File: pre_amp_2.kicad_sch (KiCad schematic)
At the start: 57 parts, among them J1 IN, J11 SW2_3, J12 SW2_1, J13 SW2_4, J14 SW5_3, J15 VR5_1, J16 OUT, J2 Vin, J3 GND, J4 VR1_1, J5 VR2_1, J6 VR1_3, J7 VR1_2, J8 SW1, J9 SW2, SW1 bright, SW2 SW_SP3T, U1 TL072, U2 ICL7660

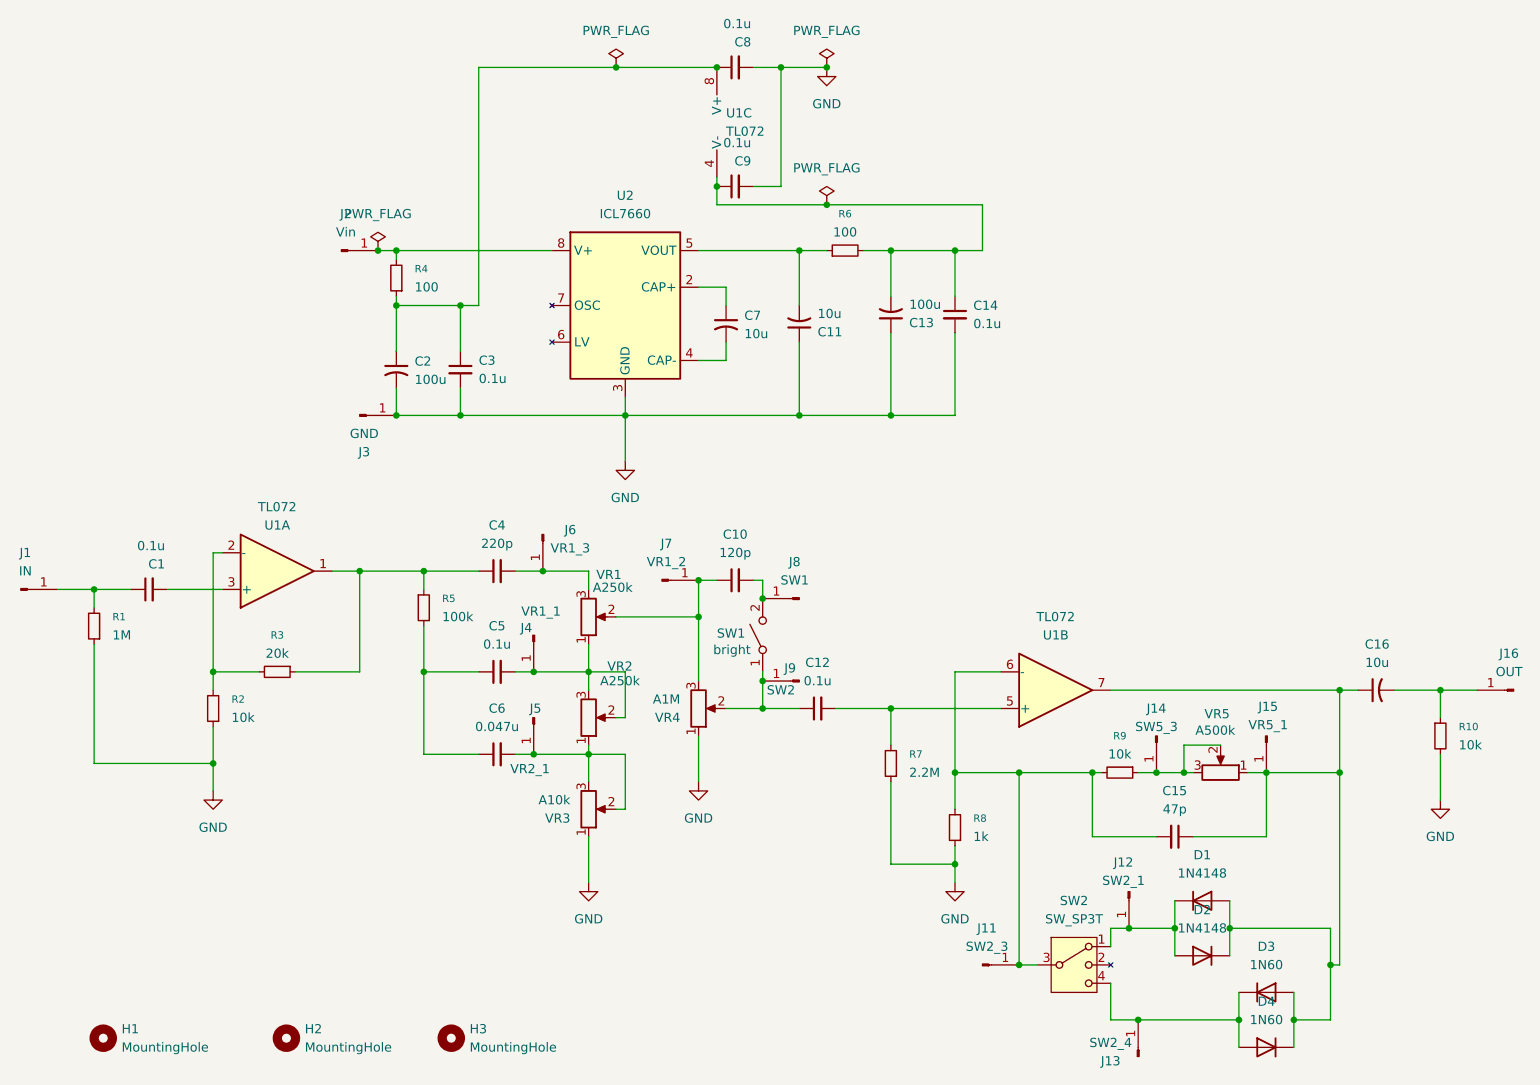
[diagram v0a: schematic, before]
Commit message: LED用の抵抗を追加
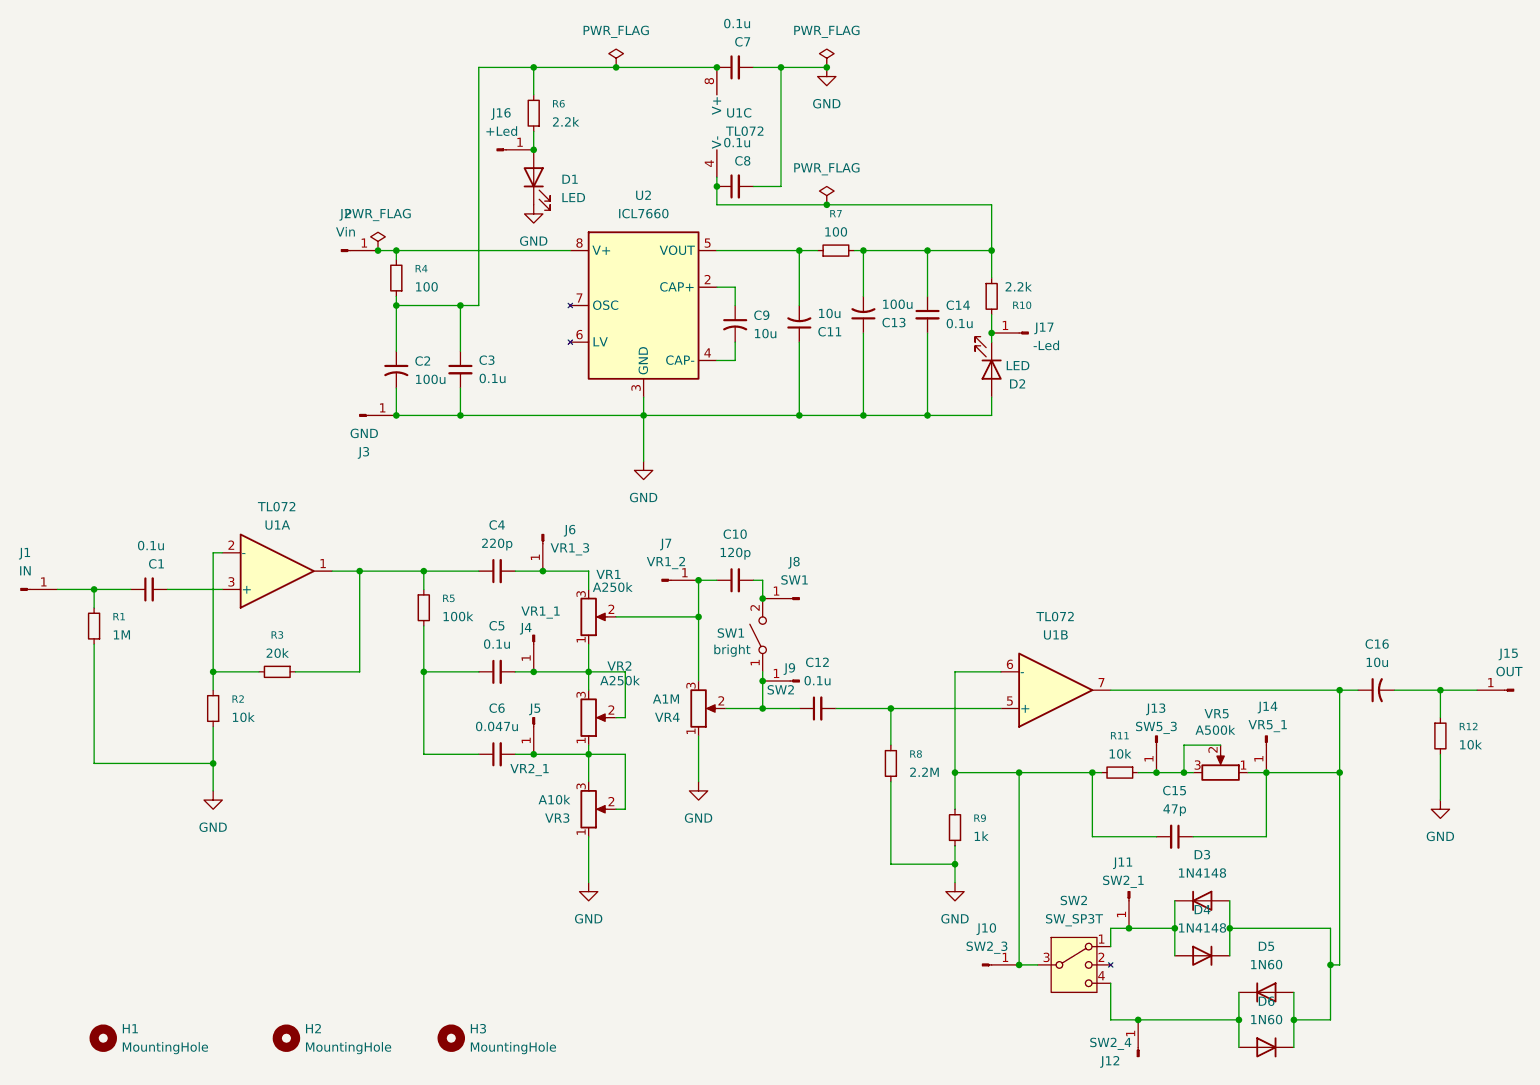
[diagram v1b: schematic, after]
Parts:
- added D1, D2: LED, symbol Device:LED
- added J16: +Led, Connector_PinHeader_2.54mm:PinHeader_1x01_P2.54mm_Vertical, symbol Connector:Conn_01x01_Pin
- added J17: -Led, Connector_PinHeader_2.54mm:PinHeader_1x01_P2.54mm_Vertical, symbol Connector:Conn_01x01_Pin
- added R10, R6: 2.2k, Resistor_THT:R_Axial_DIN0204_L3.6mm_D1.6mm_P7.62mm_Horizontal, symbol Device:R_Small
- renumbered C8 to C7, C9 to C8, C7 to C9, D1 to D3, D2 to D4, D3 to D5, D4 to D6, J11 to J10, J12 to J11, J13 to J12, J14 to J13, J15 to J14, J16 to J15, R9 to R11, R10 to R12, R6 to R7, R7 to R8, R8 to R9
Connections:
- net GND: now also D1.1 (K), D2.2 (A)
- net at C2.1, C3.1, C7.1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: now also R6.2
- net at C13.2, C14.1, C8.1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: now also R10.1
- new net: D2.1 (K), J17.1 (Pin_1), R10.2
- new net: D1.2 (A), J16.1 (Pin_1), R6.1
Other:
- moved on the sheet: C13, C14, C9, R7, U2

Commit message: 配置をやり直す
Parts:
- removed D1, D2: LED, symbol Device:LED
- removed J16: +Led, Connector_PinHeader_2.54mm:PinHeader_1x01_P2.54mm_Vertical, symbol Connector:Conn_01x01_Pin
- removed J17: -Led, Connector_PinHeader_2.54mm:PinHeader_1x01_P2.54mm_Vertical, symbol Connector:Conn_01x01_Pin
- removed R10, R6: 2.2k, Resistor_THT:R_Axial_DIN0204_L3.6mm_D1.6mm_P7.62mm_Horizontal, symbol Device:R_Small
- removed R12: 10k, Resistor_THT:R_Axial_DIN0204_L3.6mm_D1.6mm_P7.62mm_Horizontal, symbol Device:R_Small
- added J2: GND2, Connector_PinHeader_2.54mm:PinHeader_1x01_P2.54mm_Vertical, symbol Connector:Conn_01x01_Pin
- J10: renamed from J9; value SW2 -> SW1_2
- J9: renamed from J8; value SW1 -> SW1_1
- R1, R2, R3, R4, R5: footprint Resistor_THT:R_Axial_DIN0204_L3.6mm_D1.6mm_P7.62mm_Horizontal -> Resistor_THT:R_Axial_DIN0204_L3.6mm_D1.6mm_P2.54mm_Vertical
- R6: renamed from R7; footprint Resistor_THT:R_Axial_DIN0204_L3.6mm_D1.6mm_P7.62mm_Horizontal -> Resistor_THT:R_Axial_DIN0204_L3.6mm_D1.6mm_P2.54mm_Vertical
- renumbered D3 to D1, D4 to D2, D5 to D3, D6 to D4, J10 to J11, J11 to J12, J12 to J13, J13 to J14, J14 to J15, J15 to J16, J2 to J3, J3 to J4, J4 to J5, J5 to J6, J6 to J7, J7 to J8, R8 to R7, R9 to R8, R11 to R9
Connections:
- net GND: no longer R1.1, R2.1, R7.1, R8.1, VR3.1, VR4.1
- new net GND2: J2.1 (Pin_1), R1.1, R2.1, R7.1, R8.1, VR3.1, VR4.1

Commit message: 電源と入力のGNDを分離して配置を修正
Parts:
- removed J8: VR1_2, Connector_PinHeader_2.54mm:PinHeader_1x01_P2.54mm_Vertical, symbol Connector:Conn_01x01_Pin
- C10: footprint Capacitor_THT:C_Disc_D3.8mm_W2.6mm_P2.50mm -> (none)
- J13: renamed from J14; value SW5_3 -> VR5_3
- J8: renamed from J9; footprint Connector_PinHeader_2.54mm:PinHeader_1x01_P2.54mm_Vertical -> (none)
- J9: renamed from J10; footprint Connector_PinHeader_2.54mm:PinHeader_1x01_P2.54mm_Vertical -> (none)
- R4, R6: footprint Resistor_THT:R_Axial_DIN0204_L3.6mm_D1.6mm_P2.54mm_Vertical -> Resistor_THT:R_Axial_DIN0204_L3.6mm_D1.6mm_P7.62mm_Horizontal
- renumbered J11 to J10, J12 to J11, J13 to J12, J15 to J14, J16 to J15
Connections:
- net at C10.1, VR1.2, VR4.3: now also J8.1 (Pin_1)
- net at C10.2, SW1.2 (B): no longer J8.1 (Pin_1)
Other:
- moved on the sheet: J8
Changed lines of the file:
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@@
 	)
 	(junction
-		(at 123.19 95.25)
-		(diameter 0)
-		(color 0 0 0 0)
-	)
-	(junction
 		(at 182.88 138.43)
 		(diameter 0)
@@
 	)
 	(junction
-		(at 132.08 92.71)
+		(at 123.19 90.17)
 		(diameter 0)
 		(color 0 0 0 0)
@@
 	)
 	(junction
-		(at 123.19 90.17)
-		(diameter 0)
-		(color 0 0 0 0)
-	)
-	(junction
 		(at 111.76 19.05)
 		(diameter 0)
@@
 	)
 	(junction
+		(at 123.19 95.25)
+		(diameter 0)
+		(color 0 0 0 0)
+	)
+	(junction
 		(at 134.62 19.05)
 		(diameter 0)
@@
 	(wire
 		(pts
+			(xy 123.19 90.17) (xy 123.19 95.25)
+		)
+		(stroke
+			(width 0)
+			(type default)
+		)
+	)
+	(wire
+		(pts
 			(xy 111.76 19.05) (xy 125.73 19.05)
 		)
@@
 	(wire
 		(pts
+			(xy 123.19 90.17) (xy 125.73 90.17)
+		)
+		(stroke
+			(width 0)
+			(type default)
+		)
+	)
+	(wire
+		(pts
+			(xy 132.08 90.17) (xy 132.08 92.71)
+		)
+		(stroke
+			(width 0)
+			(type default)
+		)
+	)
+	(wire
+		(pts
 			(xy 49.53 91.44) (xy 57.15 91.44)
 		)
@@
 	(wire
 		(pts
-			(xy 125.73 90.17) (xy 123.19 90.17)
-		)
-		(stroke
-			(width 0)
-			(type default)
-		)
-	)
-	(wire
-		(pts
 			(xy 125.73 44.45) (xy 137.16 44.45)
 		)
@@
 	(wire
 		(pts
-			(xy 123.19 90.17) (xy 123.19 95.25)
-		)
-		(stroke
-			(width 0)
-			(type default)
-		)
-	)
-	(wire
-		(pts
 			(xy 186.69 116.84) (xy 190.5 116.84)
 		)
@@
 	(wire
 		(pts
-			(xy 132.08 92.71) (xy 132.08 90.17)
-		)
-		(stroke
-			(width 0)
-			(type default)
-		)
-	)
-	(wire
-		(pts
 			(xy 123.19 95.25) (xy 123.19 104.14)
 		)
@@
 			)
 		)
-		(property "Footprint" "Capacitor_THT:C_Disc_D3.8mm_W2.6mm_P2.50mm"
+		(property "Footprint" ""
 			(at 128.27 90.17 0)
 			(effects
@@
 		(on_board yes)
 		(dnp no)
-		(property "Reference" "J13"
+		(property "Reference" "J12"
 			(at 180.34 156.845 90)
 			(effects
@@
 			(project "pre_amp_2"
 				(path "/a24a43ce-b78c-4b02-8ea5-638bfbce1c81"
-					(reference "J13")
+					(reference "J12")
 					(unit 1)
 				)
@@
 		(on_board yes)
 		(dnp no)
-		(property "Reference" "J11"
+		(property "Reference" "J10"
 			(at 163.195 138.43 0)
 			(effects
@@
 			(project "pre_amp_2"
 				(path "/a24a43ce-b78c-4b02-8ea5-638bfbce1c81"
-					(reference "J11")
+					(reference "J10")
 					(unit 1)
 				)
@@
 		(on_board yes)
 		(dnp no)
-		(property "Reference" "J12"
+		(property "Reference" "J11"
 			(at 182.118 129.286 90)
 			(effects
@@
 			(project "pre_amp_2"
 				(path "/a24a43ce-b78c-4b02-8ea5-638bfbce1c81"
-					(reference "J12")
+					(reference "J11")
 					(unit 1)
 				)
@@
 	(symbol
 		(lib_id "Connector:Conn_01x01_Pin")
-		(at 137.16 92.71 0)
-		(mirror y)
+		(at 118.11 90.17 0)
 		(unit 1)
 		(exclude_from_sim no)
@@
 		(on_board yes)
 		(dnp no)
-		(property "Reference" "J9"
-			(at 136.525 87.63 0)
+		(property "Reference" "J8"
+			(at 118.745 85.09 0)
 			(effects
 				(font
@@
 		)
 		(property "Value" "SW1_1"
-			(at 136.525 90.17 0)
+			(at 118.745 87.63 0)
 			(effects
 				(font
@@
 			)
 		)
-		(property "Footprint" "Connector_PinHeader_2.54mm:PinHeader_1x01_P2.54mm_Vertical"
-			(at 137.16 92.71 0)
+		(property "Footprint" ""
+			(at 118.11 90.17 0)
 			(effects
 				(font
@@
 		)
 		(property "Datasheet" "~"
-			(at 137.16 92.71 0)
+			(at 118.11 90.17 0)
 			(effects
 				(font
@@
 		)
 		(property "Description" "Generic connector, single row, 01x01, script generated"
-			(at 137.16 92.71 0)
+			(at 118.11 90.17 0)
 			(effects
 				(font
@@
 			(project "pre_amp_2"
 				(path "/a24a43ce-b78c-4b02-8ea5-638bfbce1c81"
-					(reference "J9")
+					(reference "J8")
 					(unit 1)
 				)
@@
 		(on_board yes)
 		(dnp no)
-		(property "Reference" "J15"
+		(property "Reference" "J14"
 			(at 202.184 107.696 90)
 			(effects
@@
 			(project "pre_amp_2"
 				(path "/a24a43ce-b78c-4b02-8ea5-638bfbce1c81"
-					(reference "J15")
-					(unit 1)
-				)
-			)
-		)
-	)
-	(symbol
-		(lib_id "Connector:Conn_01x01_Pin")
-		(at 118.11 90.17 0)
-		(unit 1)
-		(exclude_from_sim no)
-		(in_bom yes)
-		(on_board yes)
-		(dnp no)
-		(property "Reference" "J8"
-			(at 118.745 85.09 0)
-			(effects
-				(font
-					(size 1.27 1.27)
-				)
-			)
-		)
-		(property "Value" "VR1_2"
-			(at 118.745 87.63 0)
-			(effects
-				(font
-					(size 1.27 1.27)
-				)
-			)
-		)
-		(property "Footprint" "Connector_PinHeader_2.54mm:PinHeader_1x01_P2.54mm_Vertical"
-			(at 118.11 90.17 0)
-			(effects
-				(font
-					(size 1.27 1.27)
-				)
-				(hide yes)
-			)
-		)
-		(property "Datasheet" "~"
-			(at 118.11 90.17 0)
-			(effects
-				(font
-					(size 1.27 1.27)
-				)
-				(hide yes)
-			)
-		)
-		(property "Description" "Generic connector, single row, 01x01, script generated"
-			(at 118.11 90.17 0)
-			(effects
-				(font
-					(size 1.27 1.27)
-				)
-				(hide yes)
-			)
-		)
-		(pin "1"
-		)
-		(instances
-			(project "pre_amp_2"
-				(path "/a24a43ce-b78c-4b02-8ea5-638bfbce1c81"
-					(reference "J8")
+					(reference "J14")
 					(unit 1)
 				)
@@
 			)
 		)
-		(property "Footprint" "Resistor_THT:R_Axial_DIN0204_L3.6mm_D1.6mm_P2.54mm_Vertical"
+		(property "Footprint" "Resistor_THT:R_Axial_DIN0204_L3.6mm_D1.6mm_P7.62mm_Horizontal"
 			(at 81.28 48.26 0)
 			(effects
@@
 		(on_board yes)
 		(dnp no)
-		(property "Reference" "J10"
+		(property "Reference" "J9"
 			(at 135.89 102.362 0)
 			(effects
@@
 			)
 		)
-		(property "Footprint" "Connector_PinHeader_2.54mm:PinHeader_1x01_P2.54mm_Vertical"
+		(property "Footprint" ""
 			(at 137.16 104.14 0)
 			(effects
@@
 			(project "pre_amp_2"
 				(path "/a24a43ce-b78c-4b02-8ea5-638bfbce1c81"
-					(reference "J10")
+					(reference "J9")
 					(unit 1)
 				)
@@
 		(dnp no)
 		(fields_autoplaced yes)
-		(property "Reference" "J16"
+		(property "Reference" "J15"
 			(at 235.585 100.33 0)
 			(effects
@@
 			(project "pre_amp_2"
 				(path "/a24a43ce-b78c-4b02-8ea5-638bfbce1c81"
-					(reference "J16")
+					(reference "J15")
 					(unit 1)
 				)
@@
 			)
 		)
-		(property "Footprint" "Resistor_THT:R_Axial_DIN0204_L3.6mm_D1.6mm_P2.54mm_Vertical"
+		(property "Footprint" "Resistor_THT:R_Axial_DIN0204_L3.6mm_D1.6mm_P7.62mm_Horizontal"
 			(at 142.24 44.45 0)
 			(effects
@@
 		(on_board yes)
 		(dnp no)
-		(property "Reference" "J14"
+		(property "Reference" "J13"
 			(at 186.69 107.95 90)
 			(effects
@@
 			)
 		)
-		(property "Value" "SW5_3"
+		(property "Value" "VR5_3"
 			(at 186.69 110.49 90)
 			(effects
@@
 			(project "pre_amp_2"
 				(path "/a24a43ce-b78c-4b02-8ea5-638bfbce1c81"
-					(reference "J14")
+					(reference "J13")
 					(unit 1)
 				)

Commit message: 配線の接続先を修正
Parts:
- removed J8: SW1_1, symbol Connector:Conn_01x01_Pin
- J6: value VR2_1 -> VR3_3
- J9: value SW1_2 -> VR4_2
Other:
- moved on the sheet: J9
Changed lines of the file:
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@@
 	)
 	(junction
-		(at 132.08 107.95)
-		(diameter 0)
-		(color 0 0 0 0)
-	)
-	(junction
 		(at 154.94 44.45)
 		(diameter 0)
@@
 	)
 	(junction
+		(at 132.08 107.95)
+		(diameter 0)
+		(color 0 0 0 0)
+	)
+	(junction
 		(at 107.95 102.87)
 		(diameter 0)
@@
 	)
 	(junction
-		(at 149.86 107.95)
+		(at 135.89 107.95)
 		(diameter 0)
 		(color 0 0 0 0)
 	)
 	(junction
-		(at 76.2 88.9)
+		(at 149.86 107.95)
 		(diameter 0)
 		(color 0 0 0 0)
 	)
 	(junction
-		(at 55.88 102.87)
+		(at 76.2 88.9)
 		(diameter 0)
 		(color 0 0 0 0)
 	)
 	(junction
-		(at 137.16 44.45)
+		(at 55.88 102.87)
 		(diameter 0)
 		(color 0 0 0 0)
 	)
 	(junction
-		(at 123.19 90.17)
+		(at 137.16 44.45)
 		(diameter 0)
 		(color 0 0 0 0)
@@
 	)
 	(junction
-		(at 132.08 104.14)
-		(diameter 0)
-		(color 0 0 0 0)
-	)
-	(junction
 		(at 186.69 116.84)
 		(diameter 0)
@@
 	(wire
 		(pts
-			(xy 132.08 107.95) (xy 137.16 107.95)
+			(xy 127 107.95) (xy 132.08 107.95)
 		)
 		(stroke
@@
 	(wire
 		(pts
+			(xy 132.08 102.87) (xy 132.08 107.95)
+		)
+		(stroke
+			(width 0)
+			(type default)
+		)
+	)
+	(wire
+		(pts
 			(xy 92.71 19.05) (xy 111.76 19.05)
 		)
@@
 	(wire
 		(pts
-			(xy 127 107.95) (xy 132.08 107.95)
-		)
-		(stroke
-			(width 0)
-			(type default)
-		)
-	)
-	(wire
-		(pts
 			(xy 39.37 113.03) (xy 39.37 115.57)
 		)
@@
 	(wire
 		(pts
+			(xy 135.89 107.95) (xy 137.16 107.95)
+		)
+		(stroke
+			(width 0)
+			(type default)
+		)
+	)
+	(wire
+		(pts
 			(xy 107.95 113.03) (xy 107.95 114.3)
 		)
@@
 	(wire
 		(pts
-			(xy 132.08 107.95) (xy 132.08 104.14)
-		)
-		(stroke
-			(width 0)
-			(type default)
-		)
-	)
-	(wire
-		(pts
 			(xy 90.17 67.31) (xy 115.57 67.31)
 		)
@@
 	(wire
 		(pts
-			(xy 184.15 151.13) (xy 198.12 151.13)
+			(xy 132.08 107.95) (xy 135.89 107.95)
 		)
 		(stroke
@@
 	(wire
 		(pts
-			(xy 212.09 105.41) (xy 214.63 105.41)
+			(xy 184.15 151.13) (xy 198.12 151.13)
 		)
 		(stroke
@@
 	(wire
 		(pts
-			(xy 55.88 115.57) (xy 55.88 110.49)
+			(xy 212.09 105.41) (xy 214.63 105.41)
 		)
 		(stroke
@@
 	(wire
 		(pts
-			(xy 132.08 104.14) (xy 132.08 102.87)
+			(xy 55.88 115.57) (xy 55.88 110.49)
 		)
 		(stroke
@@
 			)
 		)
-		(property "Value" "VR2_1"
+		(property "Value" "VR3_3"
 			(at 99.822 116.332 90)
 			(effects
@@
 	)
 	(symbol
-		(lib_id "Connector:Conn_01x01_Pin")
-		(at 118.11 90.17 0)
-		(unit 1)
-		(exclude_from_sim no)
-		(in_bom yes)
-		(on_board yes)
-		(dnp no)
-		(property "Reference" "J8"
-			(at 118.745 85.09 0)
-			(effects
-				(font
-					(size 1.27 1.27)
-				)
-			)
-		)
-		(property "Value" "SW1_1"
-			(at 118.745 87.63 0)
-			(effects
-				(font
-					(size 1.27 1.27)
-				)
-			)
-		)
-		(property "Footprint" ""
-			(at 118.11 90.17 0)
-			(effects
-				(font
-					(size 1.27 1.27)
-				)
-				(hide yes)
-			)
-		)
-		(property "Datasheet" "~"
-			(at 118.11 90.17 0)
-			(effects
-				(font
-					(size 1.27 1.27)
-				)
-				(hide yes)
-			)
-		)
-		(property "Description" "Generic connector, single row, 01x01, script generated"
-			(at 118.11 90.17 0)
-			(effects
-				(font
-					(size 1.27 1.27)
-				)
-				(hide yes)
-			)
-		)
-		(pin "1"
-		)
-		(instances
-			(project "pre_amp_2"
-				(path "/a24a43ce-b78c-4b02-8ea5-638bfbce1c81"
-					(reference "J8")
-					(unit 1)
-				)
-			)
-		)
-	)
-	(symbol
 		(lib_id "Device:C_Small_US")
 		(at 146.05 53.34 0)
@@
 	(symbol
 		(lib_id "Connector:Conn_01x01_Pin")
-		(at 137.16 104.14 0)
-		(mirror y)
+		(at 135.89 113.03 270)
+		(mirror x)
 		(unit 1)
 		(exclude_from_sim no)
@@
 		(dnp no)
 		(property "Reference" "J9"
-			(at 135.89 102.362 0)
+			(at 134.366 114.046 90)
 			(effects
 				(font
@@
 			)
 		)
-		(property "Value" "SW1_2"
-			(at 134.62 105.41 0)
+		(property "Value" "VR4_2"
+			(at 135.636 116.332 90)
 			(effects
 				(font
@@
 		)
 		(property "Footprint" ""
-			(at 137.16 104.14 0)
+			(at 135.89 113.03 0)
 			(effects
 				(font
@@
 		)
 		(property "Datasheet" "~"
-			(at 137.16 104.14 0)
+			(at 135.89 113.03 0)
 			(effects
 				(font
@@
 		)
 		(property "Description" "Generic connector, single row, 01x01, script generated"
-			(at 137.16 104.14 0)
+			(at 135.89 113.03 0)
 			(effects
 				(font
